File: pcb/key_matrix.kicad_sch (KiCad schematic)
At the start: 162 parts, among them K000 1.5U, K001 1U, K002 1U, K003 1U, K004 1U, K005 1U, K006 1U, K007 1U, K008 1U, K009 1U, K010 1U, K011 1U, K012 1U, K013 1.5U, K100 1.5U, K101 1U, K102 1U, K103 1U, K104 1U, K105 1U, K106 1U, K107 1U, K108 1U, K109 1U, K110 1U, K111 1U, K112 1U, K113 1.5U, K200 1.5U, K201 1U, K202 1U, K203 1U, K204 1U, K205 1U, K206 1U, K207 1U, K208 1U, K209 1U, K210 1U, K211 1U, K212 1U, K213 1.5U, K300 1.5U, K301 1U, K302 1U, K303 1U, K304 1U, K305 1U, K306 1U, K307 1U, K308 1U, K309 1U, K310 1U, K311 1U, K312 1U, K313 1.5U, K400 1.5U, K401 1U, K402 1U, K403 1U, K404 1U, K405 1U, K406 1U, K407 1U, K408 1U, K409 1U, K410 1U, K411 1U, K412 1U, K413 1.5U, U4 IS31FL3731-QF

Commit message: Switch to MiniMELF (SOD-80) diodes
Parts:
- D000, D001, D002, D003, D004, D005, D006, D007, D008, D009, D010, D011, D012, D013, D100, D101, D102, D103, D104, D105, D106, D107, D108, D109, D110, D111, D112, D113, D200, D201, D202, D203, D204, D205, D206, D207, D208, D209, D210, D211, D212, D213, D300, D301, D302, D303, D304, D305, D306, D307, D308, D309, D310, D311, D312, D313, D400, D401, D402, D403, D404, D405, D406, D407, D408, D409, D410, D411, D412, D413: footprint 0xLib_Diode_Transistor:D_SOD-323 -> 0xLib_Diode_Transistor:D_MiniMELF

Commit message: Update BOM information
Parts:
- D000, D001, D002, D003, D004, D005, D006, D007, D008, D009, D010, D011, D012, D013, D100, D101, D102, D103, D104, D105, D106, D107, D108, D109, D110, D111, D112, D113, D200, D201, D202, D203, D204, D205, D206, D207, D208, D209, D210, D211, D212, D213, D300, D301, D302, D303, D304, D305, D306, D307, D308, D309, D310, D311, D312, D313, D400, D401, D402, D403, D404, D405, D406, D407, D408, D409, D410, D411, D412, D413: LCSC C2128 -> C9808
- K000, K001, K002, K003, K004, K005, K006, K007, K008, K009, K010, K011, K012, K013, K100, K101, K102, K103, K104, K105, K106, K107, K108, K109, K110, K111, K112, K113, K200, K201, K202, K203, K204, K205, K206, K207, K208, K209, K210, K211, K212, K213, K300, K301, K302, K303, K304, K305, K306, K307, K308, K309, K310, K311, K312, K313, K400, K401, K402, K403, K404, K405, K406, K407, K408, K409, K410, K411, K412, K413, Kb106, Kb107, Kb306, Kb307, Kb402, Kb404, Kb405, Kb406, Kb408, Kb409, Kb411: now left out of the parts list

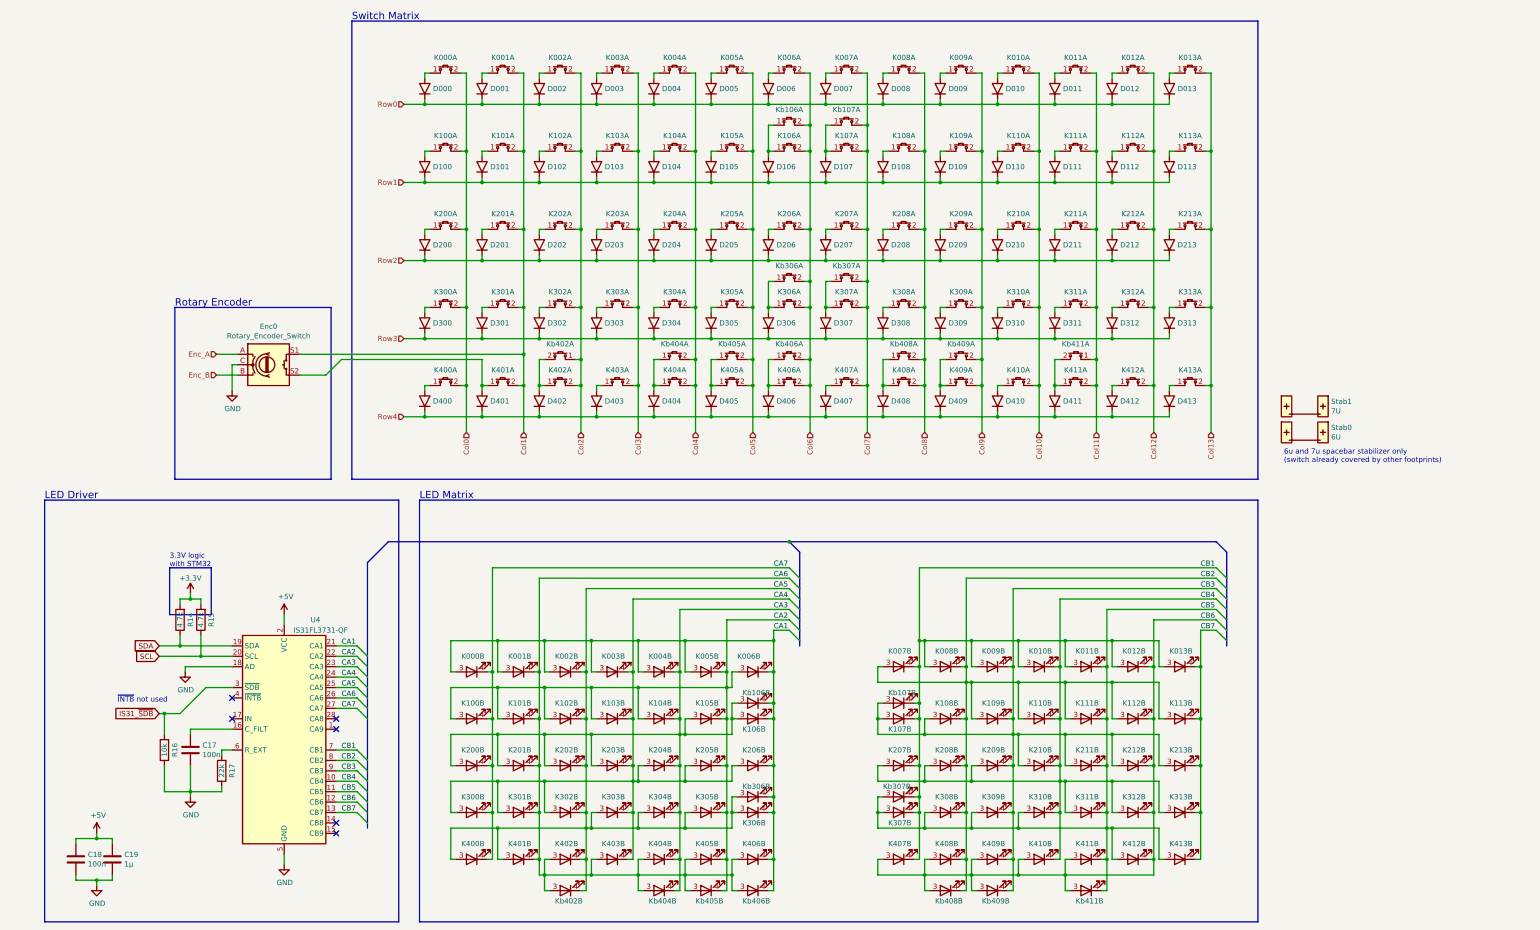
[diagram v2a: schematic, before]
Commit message: solved some schematic <> pcb inconsistencies on the encoder interface
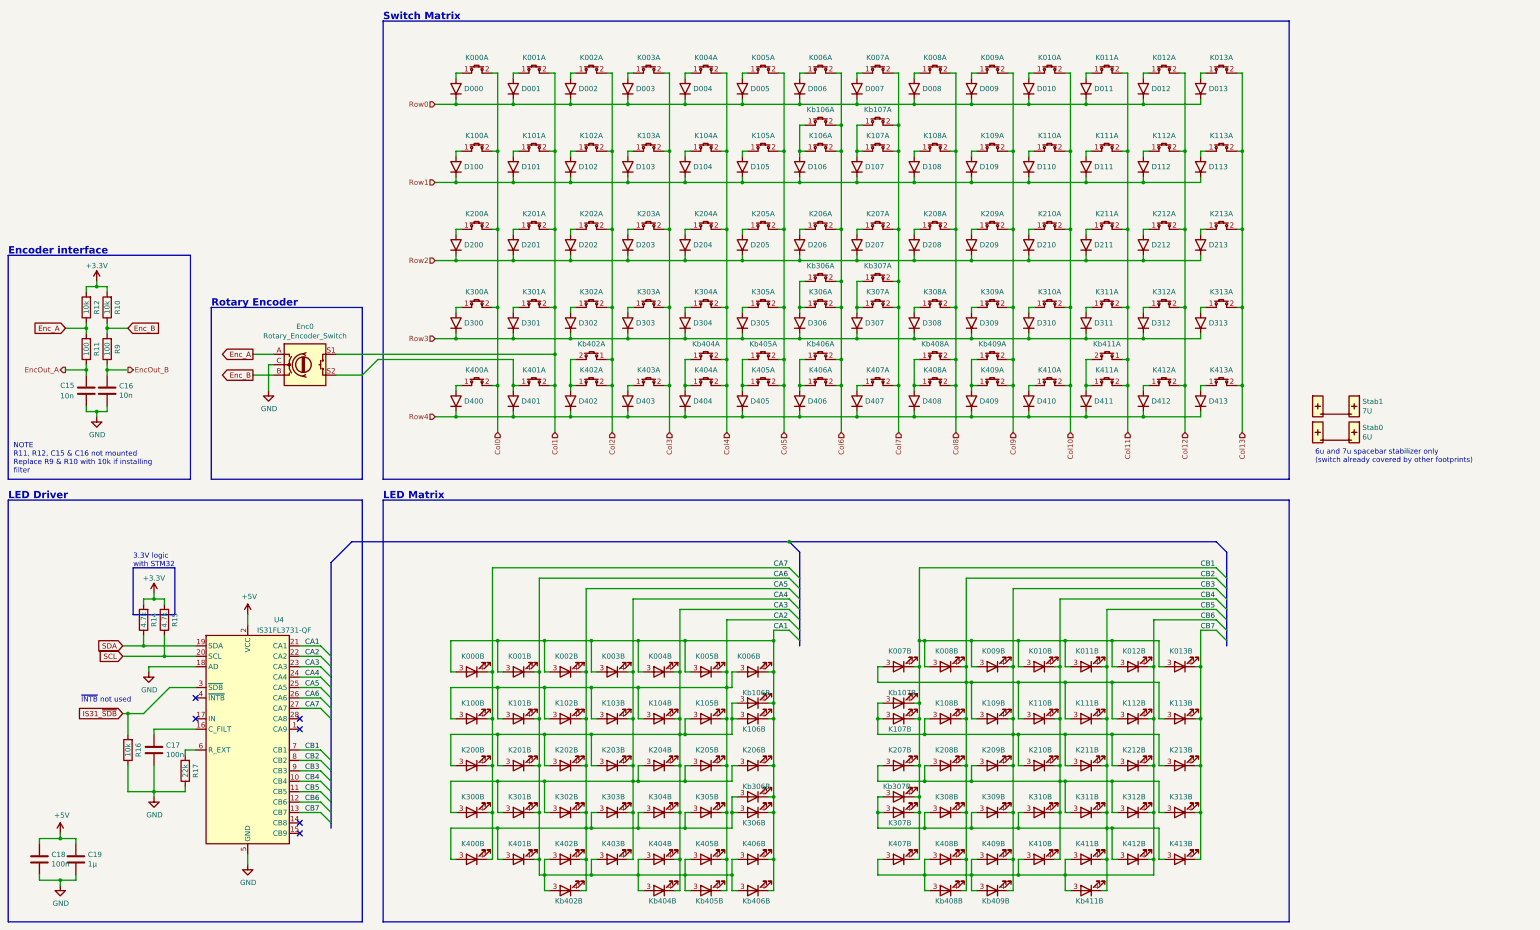
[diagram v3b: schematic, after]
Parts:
- added C15, C16: 10n, 0xLib_Passive_SMD:C_0603_1608Metric, symbol Device:C
- added R10, R12: 10k, 0xLib_Passive_SMD:R_0603_1608Metric, symbol Device:R
- added R11, R9: 100, 0xLib_Passive_SMD:R_0603_1608Metric, symbol Device:R
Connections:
- net +3.3V: now also R10.2, R12.2
- net Enc_A: now also R11.2, R12.1
- net Enc_B: now also R10.1, R9.2
- net GND: now also C15.2, C16.2
- new net EncOut_A: C15.1, R11.1
- new net EncOut_B: C16.1, R9.1
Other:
- note added: "Encoder interface"
- note added: "NOTE R11, R12, C15 & C16 not mounted Replace R9 & R10 with 10k if installing filter"
- moved on the sheet: C17, C18, C19, D000, D001, D002, D003, D004, D005, D006, D007, D008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

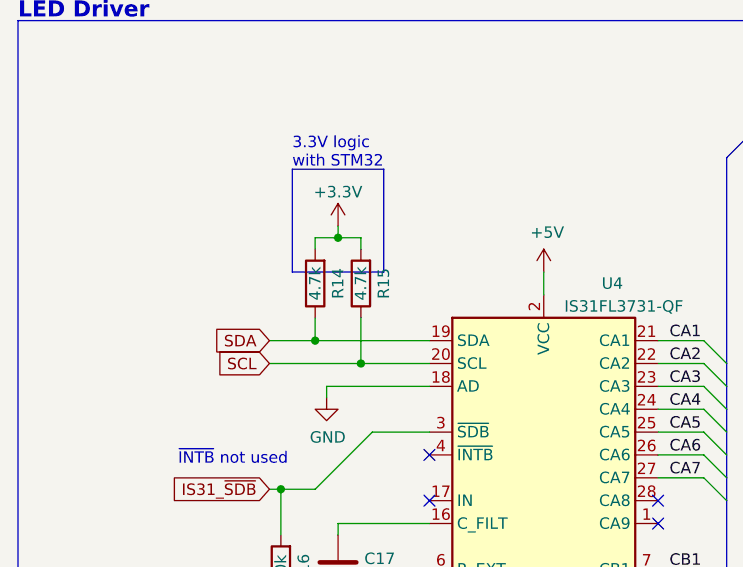
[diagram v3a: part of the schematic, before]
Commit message: Update I2C pullups + minor PCB changes
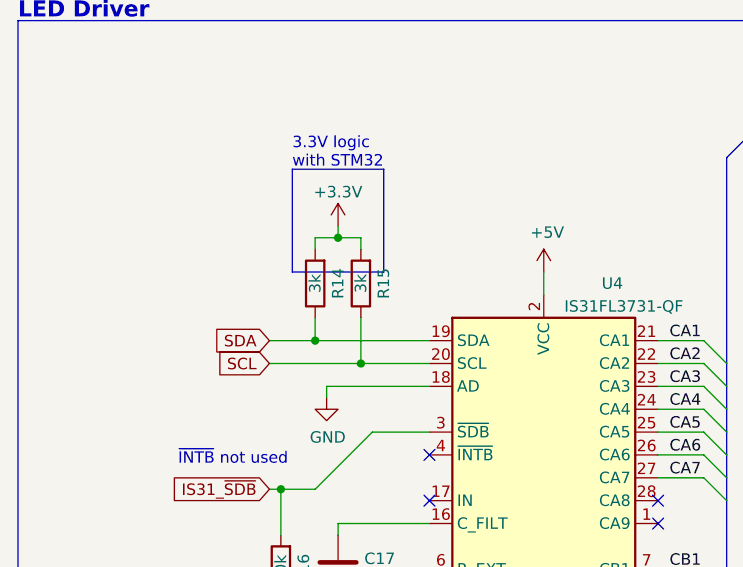
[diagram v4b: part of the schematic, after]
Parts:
- R14, R15: value 4.7k -> 3k; LCSC C23162 -> C4211
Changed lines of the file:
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@@
       (effects (font (size 1.27 1.27)))
     )
-    (property "Value" "4.7k" (at 69.85 172.72 90)
+    (property "Value" "3k" (at 69.85 172.72 90)
       (effects (font (size 1.27 1.27)))
     )
@@
       (effects (font (size 1.27 1.27)) hide)
     )
-    (property "LCSC" "C23162" (at 69.85 172.72 0)
+    (property "LCSC" "C4211" (at 69.85 172.72 0)
       (effects (font (size 1.27 1.27)) hide)
     )
@@
       (effects (font (size 1.27 1.27)))
     )
-    (property "Value" "4.7k" (at 64.77 172.72 90)
+    (property "Value" "3k" (at 64.77 172.72 90)
       (effects (font (size 1.27 1.27)))
     )
@@
       (effects (font (size 1.27 1.27)) hide)
     )
-    (property "LCSC" "C23162" (at 64.77 172.72 0)
+    (property "LCSC" "C4211" (at 64.77 172.72 0)
       (effects (font (size 1.27 1.27)) hide)
     )

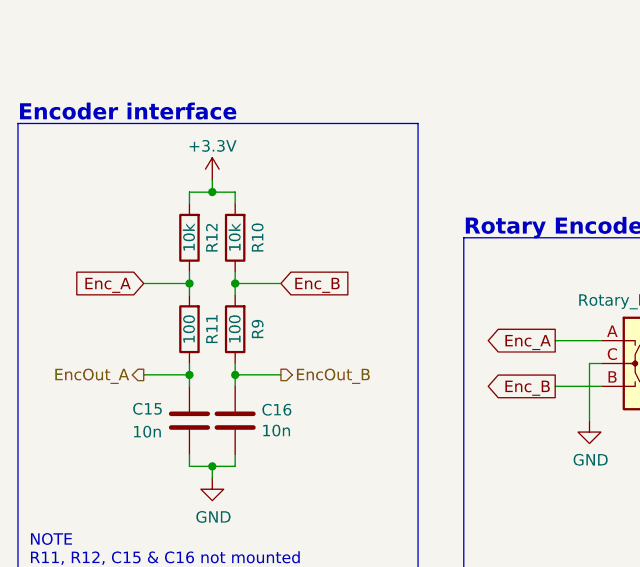
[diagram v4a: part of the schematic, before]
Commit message: Update to Kicad 8.0
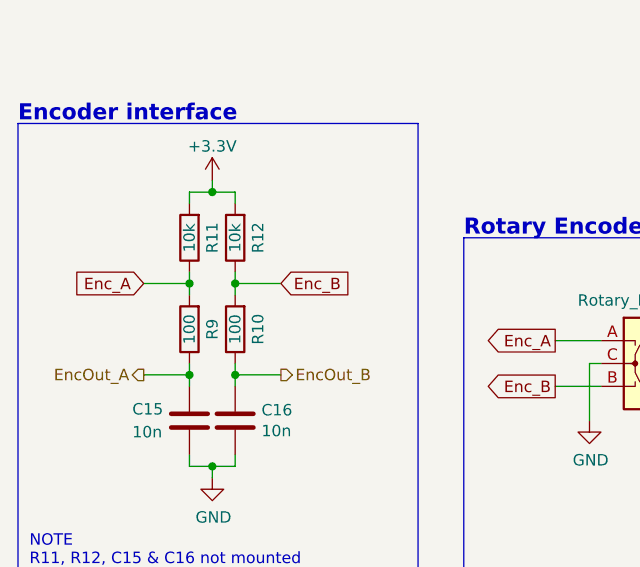
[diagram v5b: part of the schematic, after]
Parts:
- renumbered R9 to R10, R12 to R11, R10 to R12, R11 to R9
